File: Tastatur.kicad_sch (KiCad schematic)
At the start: 37 parts, among them J1 Conn_02x05_Counter_Clockwise, Q1 SI2301CDS-T1-GE3, Q2 2N7002HW, SW19 SW_SPDT, U1 CH592F, U3 AZ1117-3.3, U4 MT3608, U5 74LVC1G08, U6 LM393, U7 USBLC6-2SC6

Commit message: update power mgmt
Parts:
- removed C2: 100n, Capacitor_SMD:C_0603_1608Metric_Pad1.08x0.95mm_HandSolder, symbol Device:C
- removed C5: 10 µF, Capacitor_SMD:C_0603_1608Metric_Pad1.08x0.95mm_HandSolder, symbol #inventree:CL21A106KOQNNNE
- removed C6: 22 µF, Capacitor_SMD:C_0603_1608Metric_Pad1.08x0.95mm_HandSolder, symbol #inventree:CL21X226MOYNNWE
- removed D38, D39: CUS10S30,H3F, Diode_SMD:D_SOD-323, symbol Device:D_Schottky
- removed R1, R2: 5.1 kohm, Resistor_SMD:R_0603_1608Metric_Pad0.98x0.95mm_HandSolder, symbol #inventree:RC0603FR-075K1L
- removed U2: ~, steew:ADNS-5090, symbol steew:ADNS-5090
- removed U3: AZ1117-3.3, Package_TO_SOT_SMD:TO-252-2, symbol Regulator_Linear:AZ1117-3.3
- removed U5: 74LVC1G08, Package_TO_SOT_SMD:SOT-353_SC-70-5, symbol 74xGxx:74LVC1G08
- added C22: 100N, Capacitor_SMD:C_0603_1608Metric_Pad1.08x0.95mm_HandSolder, symbol Device:C
- added C3, C4: 22u, Capacitor_SMD:C_0603_1608Metric_Pad1.08x0.95mm_HandSolder, symbol Device:C
- added C5: 10u, Capacitor_SMD:C_0603_1608Metric_Pad1.08x0.95mm_HandSolder, symbol Device:C
- added C6: 470u, Capacitor_SMD:CP_Elec_6.3x7.7, symbol Device:C_Polarized
- added J2: XT60PW-M, Connector_AMASS:AMASS_XT60PW-M_1x02_P7.20mm_Horizontal, symbol Connector:Conn_01x02_Pin
- added L2: 4u7, Inductor_SMD:L_0603_1608Metric_Pad1.05x0.95mm_HandSolder, symbol Device:L
- added Q3, Q4, Q5: SI2301CDS-T1-GE3, Package_TO_SOT_SMD:SOT-23_Handsoldering, symbol Transistor_FET:Q_PMOS_GSD
- added R1, R2: 5k1, Resistor_SMD:R_0603_1608Metric_Pad0.98x0.95mm_HandSolder, symbol Device:R
- added R9: 0R, Resistor_SMD:R_0603_1608Metric_Pad0.98x0.95mm_HandSolder, symbol Device:R
- added U3: AP2112K-3.3, Package_TO_SOT_SMD:SOT-23-5_HandSoldering, symbol Regulator_Linear:AP2112K-3.3
- added U5: CD4052B, Package_SO:TSSOP-16_4.4x5mm_P0.65mm, symbol Analog_Switch:CD4052B
- C1: value 100n -> 100N
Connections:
- net +3.3V: now also U4.5 (IN), C3.2, C6.1, L2.1, Q3.2 (S), Q4.2 (S), Q5.3 (D)
- net +3.3VBAT: now also SW19.1 (A), Q3.3 (D)
- net +3V3USB: now also C4.1, Q4.3 (D), U3.5 (VOUT)
- net D+: now also U1.12 (UD+)
- net D-: now also U1.13 (UD-)
- net GND: now also SW19.3 (C), U4.2 (GND), C22.2, C3.1, C4.2, C5.2, C6.2, J2.2 (Pin_2), Q3.1 (G), Q4.1 (G), Q5.1 (G), R1.2, R2.2, U3.2 (GND), U5.1 (Y0), U5.2 (Y2), U5.3 (Y), U5.4 (Y3), U5.5 (Y1), U5.7 (VEE), U5.8 (VSS)
- net at F1.1, L1.2, TP3.1: now also C5.1
- net at USB1.4 (CC1): now also R2.1
- net at F1.2, TP4.1: now also R9.1, U3.1 (VIN)
- net at AE1.1 (A): now also U1.21 (ANT)
- net LEDTOGGLE: now reaches U4.4 (EN)
- net LEDTOGGLE: now also SW19.2 (B)
- net at USB1.10 (CC2): now also R1.1
- net LEDDATA: now reaches U1.15 (PB4)
- net LEDDATA: now also U5.13 (X)
- net LEDSEL0: now reaches U1.23 (PA4)
- net LEDSEL0: now also U5.10 (A)
- net LEDSEL1: now reaches U1.6 (PA8)
- net LEDSEL1: now also U5.9 (B)
- net at U4.1 (SW): now also L2.2
- new net: J2.1 (Pin_1), Q5.2 (S)
- new net: R9.2, U3.3 (EN)
- new net +5V: C22.1, U5.16 (VDD)
- new net LEDSWITCH: U5.6 (INH)
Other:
- sheet Matrix ports: added LEDDATA0, LEDDATA1, LEDDATA2, LEDDATA3; removed LED_DRIVE
- note added: "Hot swap stabilization"
- note added: "LED Battery Boost"
- note added: "LED Row Mux"
- note added: "LED Toggle Switch"
- note added: "Split X60"
- moved on the sheet: AE1, J1, SW19, TP1, U1, U4

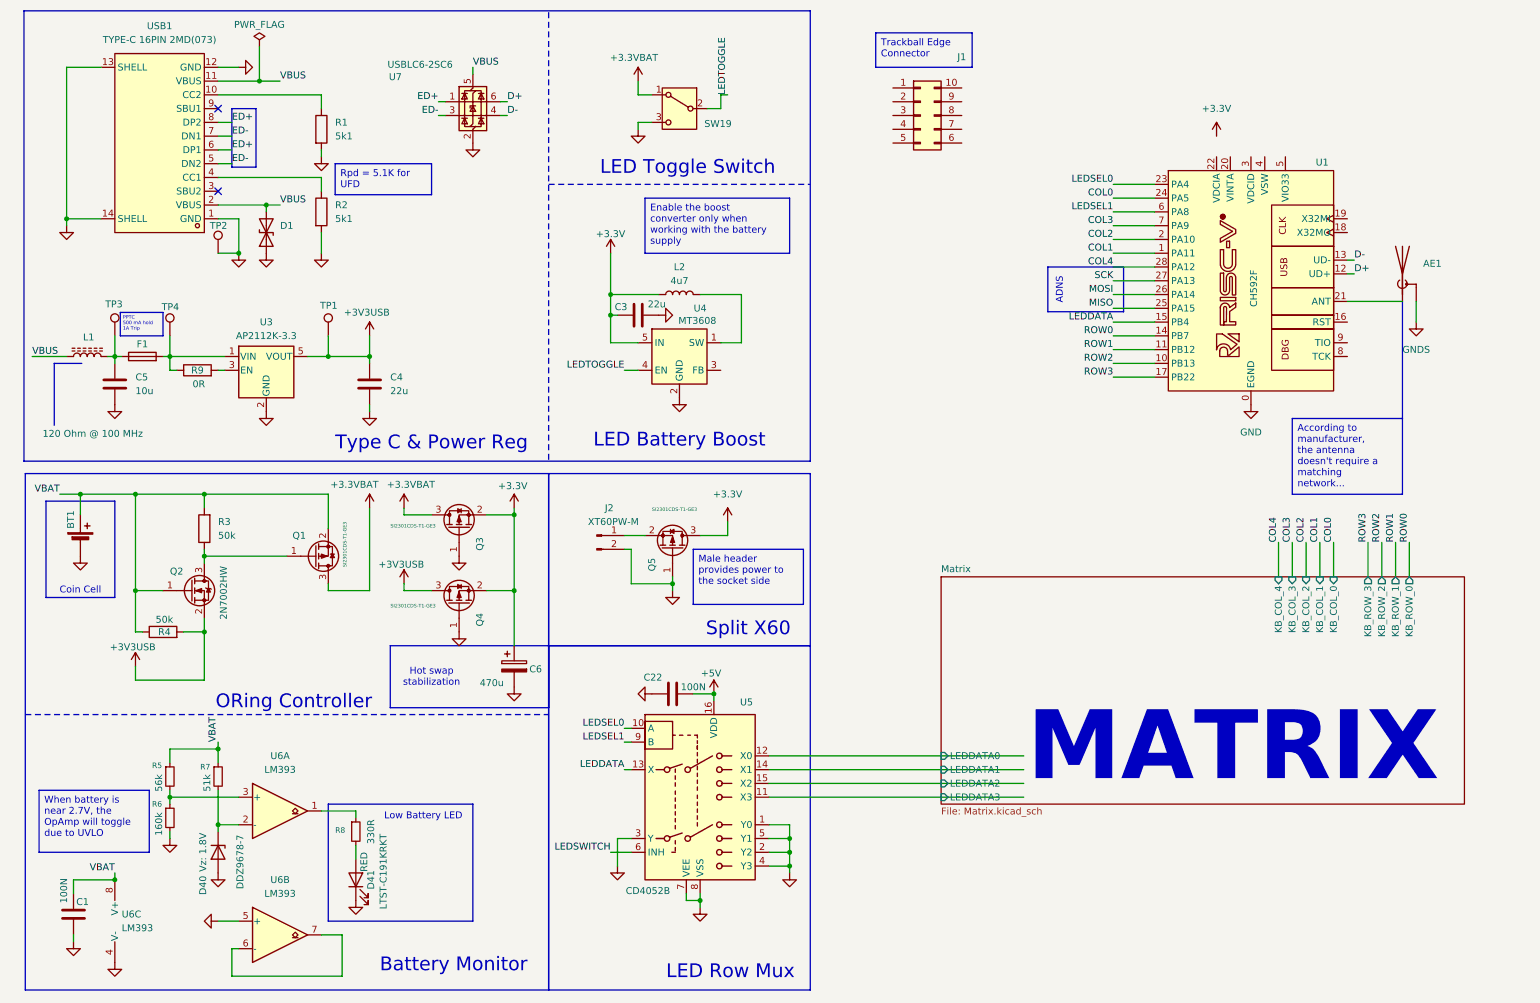
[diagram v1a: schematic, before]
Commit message: finish preliminary schematic
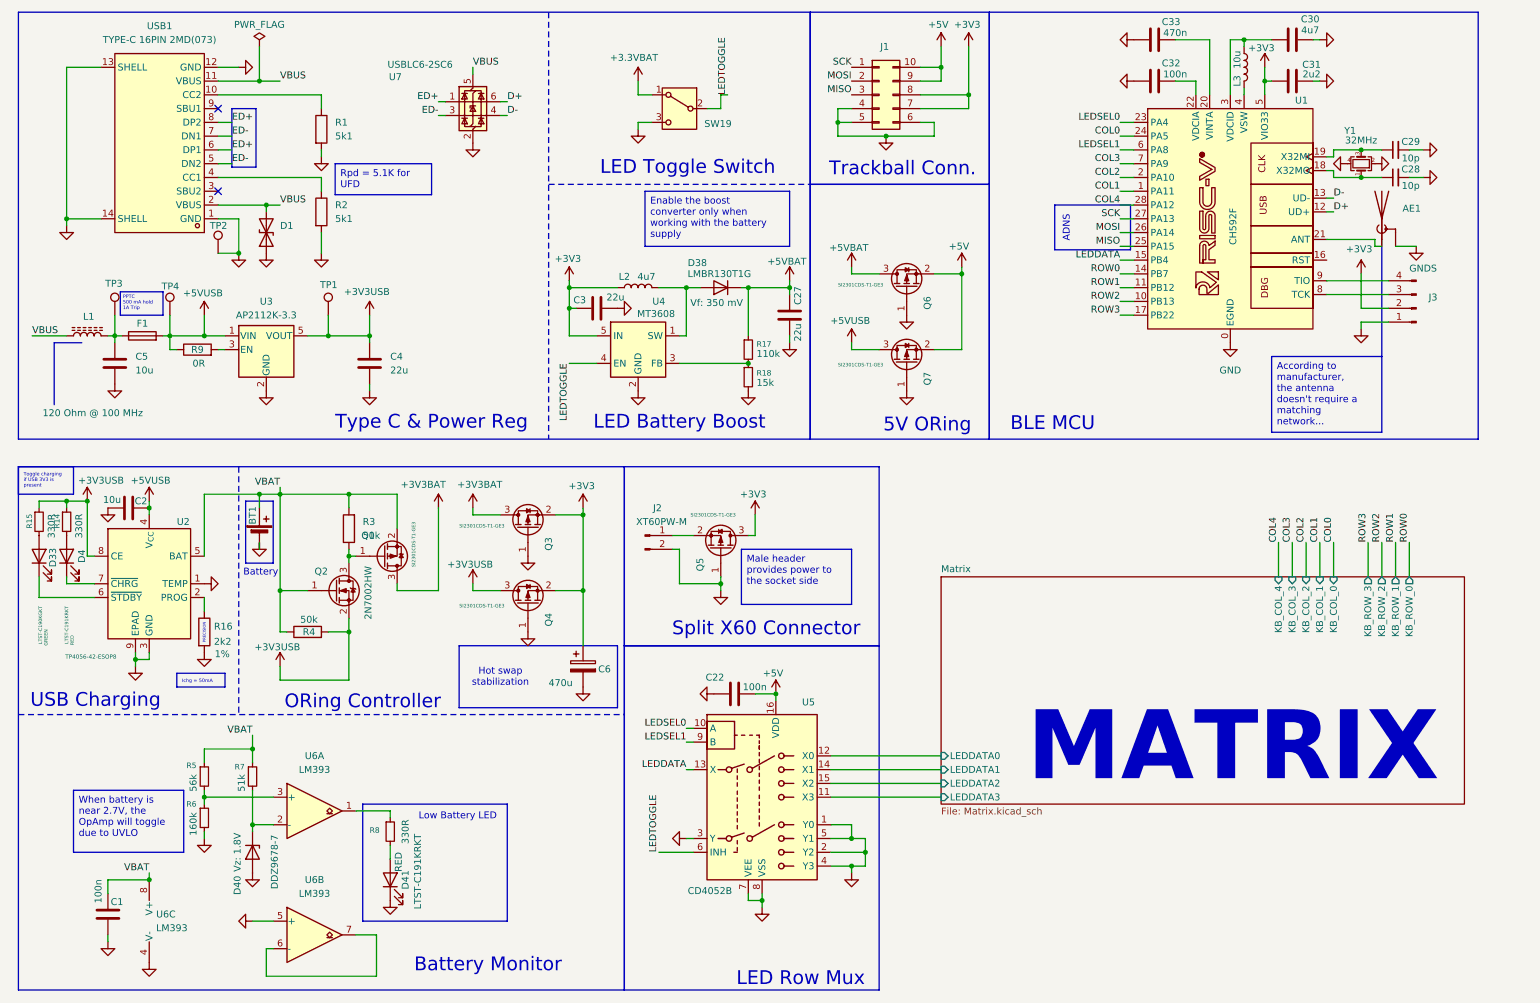
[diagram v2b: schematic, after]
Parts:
- added C2: 10u, Capacitor_SMD:C_0603_1608Metric_Pad1.08x0.95mm_HandSolder, symbol Device:C
- added C27: 22u, Capacitor_SMD:C_0603_1608Metric_Pad1.08x0.95mm_HandSolder, symbol Device:C
- added C28, C29: 10p, Capacitor_SMD:C_0603_1608Metric_Pad1.08x0.95mm_HandSolder, symbol Device:C_Small
- added C30: 4u7, Capacitor_SMD:C_0603_1608Metric_Pad1.08x0.95mm_HandSolder, symbol Device:C
- added C31: 2u2, Capacitor_SMD:C_0603_1608Metric_Pad1.08x0.95mm_HandSolder, symbol Device:C
- added C32: 100n, Capacitor_SMD:C_0603_1608Metric_Pad1.08x0.95mm_HandSolder, symbol Device:C
- added C33: 470n, Capacitor_SMD:C_0603_1608Metric_Pad1.08x0.95mm_HandSolder, symbol Device:C
- added D33: GREEN, LED_SMD:LED_0603_1608Metric, symbol Device:LED
- added D38: LMBR130T1G, Diode_SMD:D_SOD-123, symbol Device:D
- added D4: RED, LED_SMD:LED_0603_1608Metric, symbol Device:LED
- added J3: Conn_01x04_Pin, Connector_JST:JST_PH_B4B-PH-K_1x04_P2.00mm_Vertical, symbol Connector:Conn_01x04_Pin
- added L3: 10u, Inductor_SMD:L_0603_1608Metric_Pad1.05x0.95mm_HandSolder, symbol Device:L
- added Q6, Q7: SI2301CDS-T1-GE3, Package_TO_SOT_SMD:SOT-23_Handsoldering, symbol Transistor_FET:Q_PMOS_GSD
- added R14, R15: 330R, Resistor_SMD:R_0603_1608Metric_Pad0.98x0.95mm_HandSolder, symbol Device:R_Small
- added R16: 2k2, Resistor_SMD:R_0603_1608Metric_Pad0.98x0.95mm_HandSolder, symbol Device:R
- added R17: 110k, Resistor_SMD:R_0603_1608Metric_Pad0.98x0.95mm_HandSolder, symbol Device:R_Small
- added R18: 15k, Resistor_SMD:R_0603_1608Metric_Pad0.98x0.95mm_HandSolder, symbol Device:R_Small
- added U2: TP4056-42-ESOP8, Package_TO_SOT_SMD:TSOT-23-6_HandSoldering, symbol Battery_Management:TP4056-42-ESOP8
- added Y1: 32MHz, Crystal:Crystal_SMD_2016-4Pin_2.0x1.6mm, symbol Device:Crystal_GND24_Small
- C1, C22: value 100N -> 100n
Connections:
- net +3.3V is gone; now on net +3V3: C3.2, C6.1, L2.1, Q3.2 (S), Q4.2 (S), Q5.3 (D), U4.5 (IN)
- net LEDSWITCH is gone; now on net LEDTOGGLE: U5.6 (INH)
- net +3.3VBAT: no longer Q1.3 (D), Q3.3 (D)
- net +3V3USB: now also R14.1, R15.1, U2.8 (CE)
- net +5V: now also J1.10 (Pin_10), J1.9 (Pin_9), Q6.2 (S), Q7.2 (S)
- net GND: now also J1.4 (Pin_4), J1.5 (Pin_5), J1.6 (Pin_6), C2.1, C27.1, C28.2, C29.2, C30.2, C31.2, C32.1, C33.1, J3.1 (Pin_1), Q6.1 (G), Q7.1 (G), R16.2, R18.2, U2.1 (TEMP), U2.3 (GND), U2.9 (EPAD), Y1.2, Y1.4
- net MISO: now also J1.3 (Pin_3)
- net MOSI: now also J1.2 (Pin_2)
- net Matrix/LEDDATA0: now also U5.12 (X0)
- net Matrix/LEDDATA1: now also U5.14 (X1)
- net Matrix/LEDDATA2: now also U5.15 (X2)
- net Matrix/LEDDATA3: now also U5.11 (X3)
- net SCK: now also J1.1 (Pin_1)
- net VBAT: now also U2.5 (BAT)
- net +5VUSB: now reaches F1.2, R9.1, TP4.1, U3.1 (VIN)
- net +5VUSB: now also C2.2, Q7.3 (D), U2.4 (V_{CC})
- net +3V3: now reaches J1.7 (Pin_7)
- net +3V3: now also J1.8 (Pin_8), U1.5 (VIO33), C31.1, J3.2 (Pin_2)
- net at U1.18 (X32MO): now also C28.1, Y1.1
- net at U1.19 (X32MI): now also C29.1, Y1.3
- net at U1.20 (VINTA): now also C33.2
- net at U1.22 (VDCIA): now also C32.2
- net at U1.3 (VDCID): now also C30.1, L3.1
- net at U1.4 (VSW): now also L3.2
- net at U1.8 (TCK): now also J3.3 (Pin_3)
- net at U1.9 (TIO): now also J3.4 (Pin_4)
- net at L2.2, U4.1 (SW): now also D38.2 (A)
- net at U4.3 (FB): now also R17.2, R18.1
- new net: R16.1, U2.2 (PROG)
- new net: D33.1 (K), U2.6 (~{STDBY})
- new net: D4.1 (K), U2.7 (~{CHRG})
- new net: D4.2 (A), R14.2
- new net: D33.2 (A), R15.2
- new net +3V3BAT: Q1.3 (D), Q3.3 (D)
- new net +5VBAT: C27.2, D38.1 (K), Q6.3 (D), R17.1
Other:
- note added: "5V ORing"
- note added: "BLE MCU"
- note added: "Battery"
- note added: "PRECISION"
- note added: "Split X60 Connector"
- note added: "Trackball Conn."
- note added: "USB Charging"
- note removed: "Coin Cell"
- note removed: "Split X60"
- moved on the sheet: AE1, BT1, C1, C22, C3, C4, C5, C6, D40, D41, F1, J1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

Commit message: amend UVLO values
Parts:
- R5: value 56k -> 33k
- R6: value 160k -> 56k
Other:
- company: (none) -> Daniel (steewBSD)
- title: (none) -> Tastatur the BLE Keyboard
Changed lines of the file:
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@@
 	(generator_version "9.0")
 	(paper "A4")
+	(title_block
+		(title "Tastatur the BLE Keyboard")
+		(date "2025-07-18")
+		(rev "0")
+		(company "Daniel (steewBSD)")
+	)
 	(rectangle
 		(start 125.73 132.08)
@@
 		)
 	)
-	(text_box "When battery is near 2.7V, the OpAmp will toggle due to UVLO"
+	(text_box "When battery is near 2.9V, the OpAmp will toggle due to UVLO"
 		(exclude_from_sim no)
 		(at 24.13 158.75 0)
@@
 			)
 		)
-		(property "Value" "56k"
+		(property "Value" "33k"
 			(at 46.228 159.004 90)
 			(effects
@@
 		(dnp no)
 		(property "Reference" "R6"
-			(at 44.958 161.29 0)
+			(at 44.958 162.052 0)
 			(effects
 				(font
@@
 			)
 		)
-		(property "Value" "160k"
+		(property "Value" "56k"
 			(at 46.228 167.132 90)
 			(effects
@@
 	(sheet
 		(at 184.15 119.38)
-		(size 96.52 41.91)
+		(size 96.52 43.18)
 		(exclude_from_sim no)
 		(in_bom yes)
@@
 		)
 		(property "Sheetfile" "Matrix.kicad_sch"
-			(at 184.15 161.8746 0)
+			(at 184.15 163.1446 0)
 			(effects
 				(font

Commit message: finish initial placement
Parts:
- removed SW19: SW_SPDT, symbol Switch:SW_SPDT
- removed TP3: TestPoint, TestPoint:TestPoint_Pad_D1.0mm, symbol Connector:TestPoint
- added H201, H202: MountingHole, MountingHole:MountingHole_2.2mm_M2_ISO7380, symbol Mechanical:MountingHole
- added R205: 50k, Resistor_SMD:R_0603_1608Metric_Pad0.98x0.95mm_HandSolder, symbol Device:R
- added SW221: MK-12C02-G020, Button_Switch_SMD:SW_SPDT_PCM12, symbol Switch:SW_SPDT_312
- AE101: renamed from AE1; footprint (none) -> Inductor_SMD:L_1206_3216Metric
- BT101: renamed from BT1; footprint (none) -> Battery:BatteryHolder_Keystone_1058_1x2032
- renumbered C33 to C101, C30 to C102, C32 to C103, C31 to C104, C29 to C105, C28 to C106, C3 to C107, C27 to C108, C5 to C109, C4 to C110, C2 to C111, C6 to C112, C22 to C113, C1 to C114, D1 to D101, D38 to D102, D33 to D103, D4 to D104, D40 to D105, D41 to D106, F1 to F101, J1 to J101, J3 to J102, J2 to J103, L3 to L101, L2 to L102, L1 to L103, Q6 to Q101, Q7 to Q102, Q3 to Q103, Q5 to Q104, Q1 to Q105, Q2 to Q106, Q4 to Q107, R1 to R101, R2 to R102, R9 to R103, R17 to R104, R18 to R105, R15 to R106, R14 to R107, R3 to R108, R16 to R109, R4 to R110, R5 to R111, R7 to R112, R6 to R113, R8 to R114, TP2 to TP101, TP4 to TP103, TP1 to TP104, U7 to U101, U1 to U102, U3 to U103, U4 to U104, U2 to U105, U5 to U106, U6 to U107, USB1 to USB101, Y1 to Y101
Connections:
- net +3.3VBAT: now also SW221.2 (C)
- net GND: now also U102.16 (RST), R205.2, SW221.3 (A)
- net LEDTOGGLE: now also R205.1, SW221.1 (B)

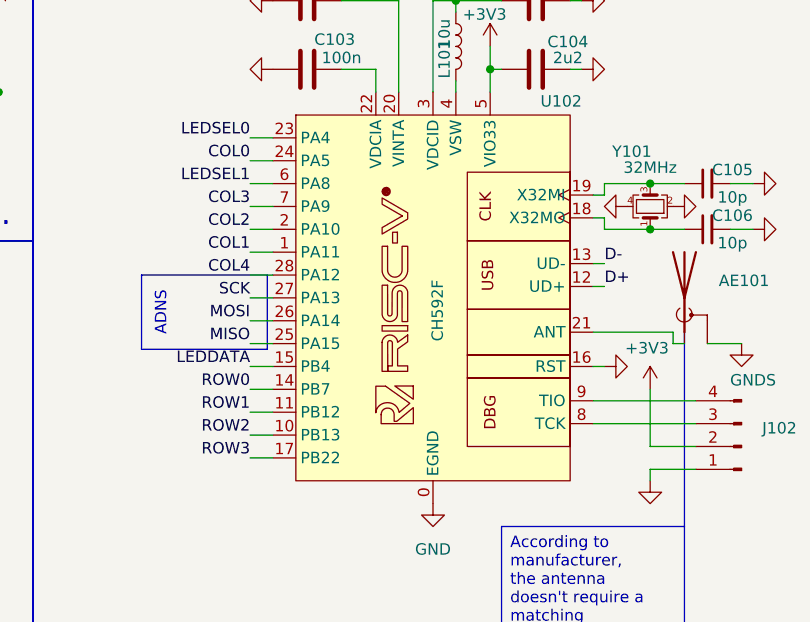
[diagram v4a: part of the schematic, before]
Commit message: start routing power
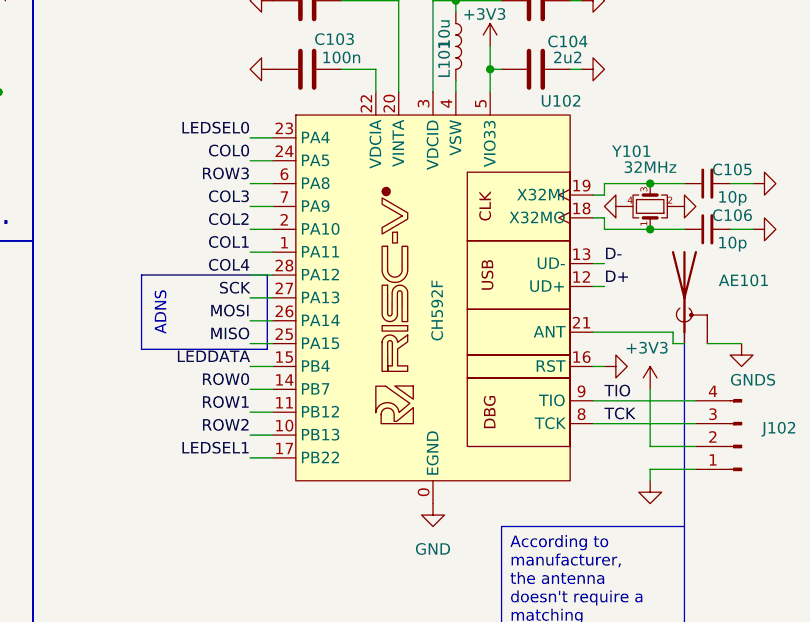
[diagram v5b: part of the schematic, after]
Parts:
- U105: footprint Package_TO_SOT_SMD:TSOT-23-6_HandSoldering -> Package_SO:SOP-8-1EP_4.57x4.57mm_P1.27mm_EP4.57x4.45mm
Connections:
- net LEDSEL1: now also U102.17 (PB22); no longer U102.6 (PA8)
- net ROW3: now also U102.6 (PA8); no longer U102.17 (PB22)
- net TCK: now reaches J102.3 (Pin_3), U102.8 (TCK)
- net TIO: now reaches J102.4 (Pin_4), U102.9 (TIO)
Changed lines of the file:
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@@
 	(wire
 		(pts
+			(xy 217.17 40.64) (xy 219.71 40.64)
+		)
+		(stroke
+			(width 0)
+			(type default)
+		)
+	)
+	(wire
+		(pts
 			(xy 62.23 138.43) (xy 74.93 138.43)
 		)
@@
 	(wire
 		(pts
-			(xy 217.17 40.64) (xy 219.71 40.64)
-		)
-		(stroke
-			(width 0)
-			(type default)
-		)
-	)
-	(wire
-		(pts
 			(xy 148.59 179.07) (xy 151.13 179.07)
 		)
@@
 	(wire
 		(pts
+			(xy 217.17 71.12) (xy 219.71 71.12)
+		)
+		(stroke
+			(width 0)
+			(type default)
+		)
+	)
+	(wire
+		(pts
 			(xy 254 113.03) (xy 254 119.38)
 		)
@@
 		)
 	)
-	(wire
-		(pts
-			(xy 217.17 71.12) (xy 219.71 71.12)
-		)
-		(stroke
-			(width 0)
-			(type default)
-		)
-	)
 	(polyline
 		(pts
@@
 		)
 	)
-	(label "ROW3"
-		(at 217.17 71.12 180)
-		(effects
-			(font
-				(size 1.27 1.27)
-			)
-			(justify right bottom)
-		)
-	)
 	(label "ROW2"
 		(at 265.43 113.03 90)
@@
 		)
 	)
+	(label "LEDSEL1"
+		(at 217.17 71.12 180)
+		(effects
+			(font
+				(size 1.27 1.27)
+			)
+			(justify right bottom)
+		)
+	)
 	(label "ROW0"
 		(at 270.51 113.03 90)
@@
 		)
 	)
+	(label "ROW3"
+		(at 217.17 40.64 180)
+		(effects
+			(font
+				(size 1.27 1.27)
+			)
+			(justify right bottom)
+		)
+	)
+	(label "TCK"
+		(at 256.54 67.31 0)
+		(effects
+			(font
+				(size 1.27 1.27)
+			)
+			(justify left bottom)
+		)
+	)
 	(label "VBUS"
 		(at 62.23 50.8 0)
@@
 		)
 	)
-	(label "LEDSEL1"
-		(at 217.17 40.64 180)
+	(label "TIO"
+		(at 256.54 64.77 0)
 		(effects
 			(font
 				(size 1.27 1.27)
 			)
-			(justify right bottom)
+			(justify left bottom)
 		)
 	)
@@
 			)
 		)
-		(property "Footprint" "Package_TO_SOT_SMD:TSOT-23-6_HandSoldering"
+		(property "Footprint" "Package_SO:SOP-8-1EP_4.57x4.57mm_P1.27mm_EP4.57x4.45mm"
 			(at 38.608 143.51 0)
 			(effects

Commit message: halfway new routing
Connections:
- net +3.3VBAT is gone; now on net +3V3BAT: SW221.2 (C)
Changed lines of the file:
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@@
 			)
 		)
-		(property "Value" "+3.3VBAT"
+		(property "Value" "+3V3BAT"
 			(at 122.428 22.352 0)
 			(effects
